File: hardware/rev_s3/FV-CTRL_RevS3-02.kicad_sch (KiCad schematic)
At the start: 10 parts, among them J21 USB_C_16P, SW1 RESET, SW2 BOOT, U1 ESP32-S3-WROOM-1U

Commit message: fix: raise Rev-S3 minimum drill to 0.3 mm
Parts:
- U1: footprint RF_Module:ESP32-S3-WROOM-1U -> fv_rev_s3:ESP32-S3-WROOM-1U_0p3
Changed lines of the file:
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@@
 			(effects (font (size 1.27 1.27)))
 		)
-		(property "Footprint" "RF_Module:ESP32-S3-WROOM-1U"
+		(property "Footprint" "fv_rev_s3:ESP32-S3-WROOM-1U_0p3"
 			(at 203.2000 101.6000 0)
 			(effects (font (size 1.27 1.27)) (hide yes))

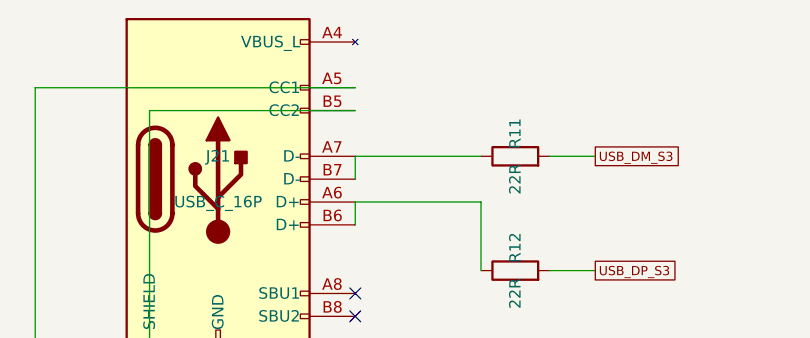
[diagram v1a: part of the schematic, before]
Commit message: fix: align Rev-S3 USB-C VBUS schematic parity
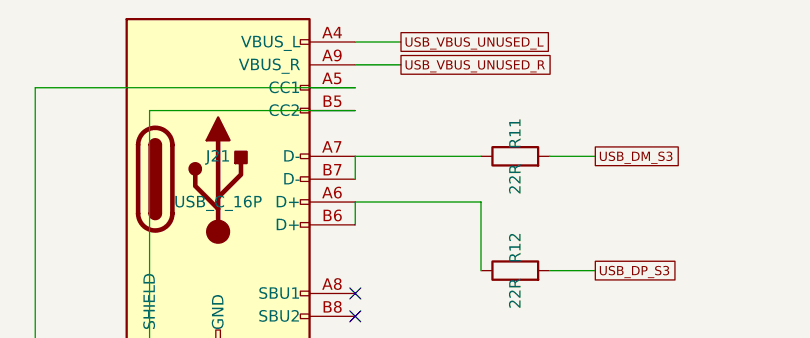
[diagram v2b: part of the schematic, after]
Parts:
- J21: symbol Connector:USB_C_Receptacle_USB2.0_16P -> fv_rev_s3:USB_C_Receptacle_USB2.0_16P_VBUS_UNUSED
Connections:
- net USB_VBUS_UNUSED_L: now reaches J21.A4 (VBUS_L), J21.B9 (VBUS_L)
- net USB_VBUS_UNUSED_L: no longer J21.A9 (VBUS_R), J21.B4 (VBUS_R)
- new net USB_VBUS_UNUSED_R: J21.A9 (VBUS_R), J21.B4 (VBUS_R)
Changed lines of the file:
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@@
 	(global_label "GND" (shape passive) (at 208.2800 129.5400 0) (effects (font (size 1.016 1.016)) (justify left)))
 	(symbol
-		(lib_id "Connector:USB_C_Receptacle_USB2.0_16P")
+		(lib_id "fv_rev_s3:USB_C_Receptacle_USB2.0_16P_VBUS_UNUSED")
 		(at 63.5000 63.5000 0)
 		(unit 1)
@@
 		)
 	)
+	(wire
+		(pts (xy 78.7400 48.2600) (xy 83.8200 48.2600))
+		(stroke (width 0) (type default))
+	)
+	(global_label "USB_VBUS_UNUSED_L" (shape passive) (at 83.8200 48.2600 0) (effects (font (size 1.016 1.016)) (justify left)))
+	(wire
+		(pts (xy 78.7400 50.8000) (xy 83.8200 50.8000))
+		(stroke (width 0) (type default))
+	)
+	(global_label "USB_VBUS_UNUSED_R" (shape passive) (at 83.8200 50.8000 0) (effects (font (size 1.016 1.016)) (justify left)))
 	(global_label "GND" (shape passive) (at 58.4200 86.3600 180) (effects (font (size 1.016 1.016)) (justify right)))
 	(wire
